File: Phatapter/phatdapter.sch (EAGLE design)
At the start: 16 parts, among them J1 RASPBERRYPI-40-PIN-GPIO_SMD_M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, J2 RASPBERRYPI-40-PIN-GPIO_RIGHT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, J3 QWIIC_RIGHT_ANGLE, J5 QWIIC_RIGHT_ANGLE

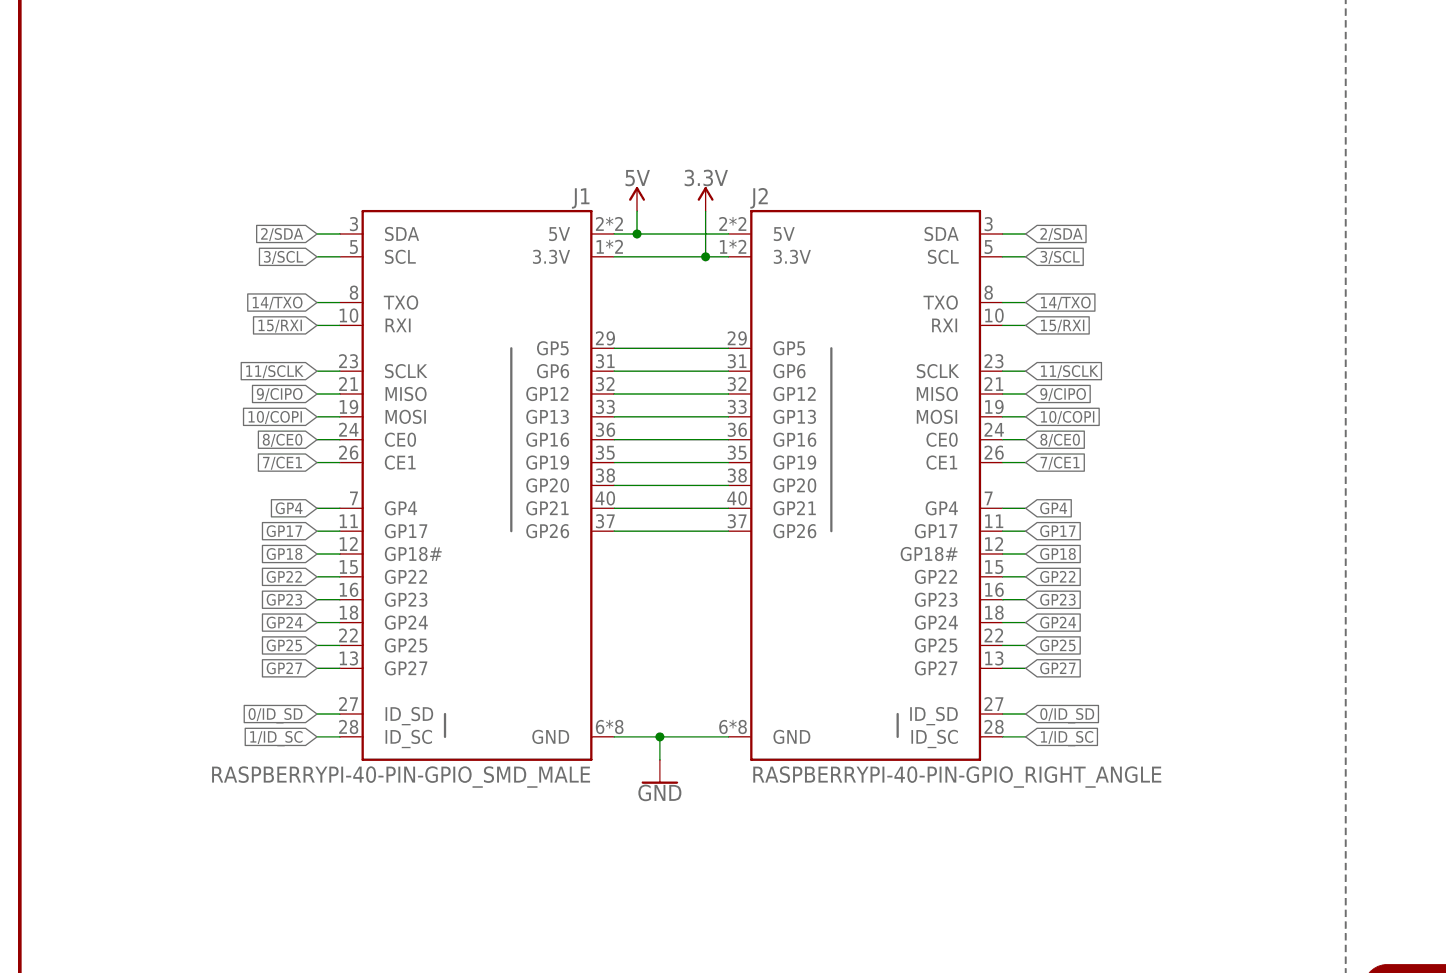
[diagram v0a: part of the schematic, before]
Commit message: Updates symbol which required an entire reroute of the board
* Adds "qwiic mount" silk
* moves Qwiic connector "lower" on the board to align with standoffs
* Adds standoffs for micro-hats
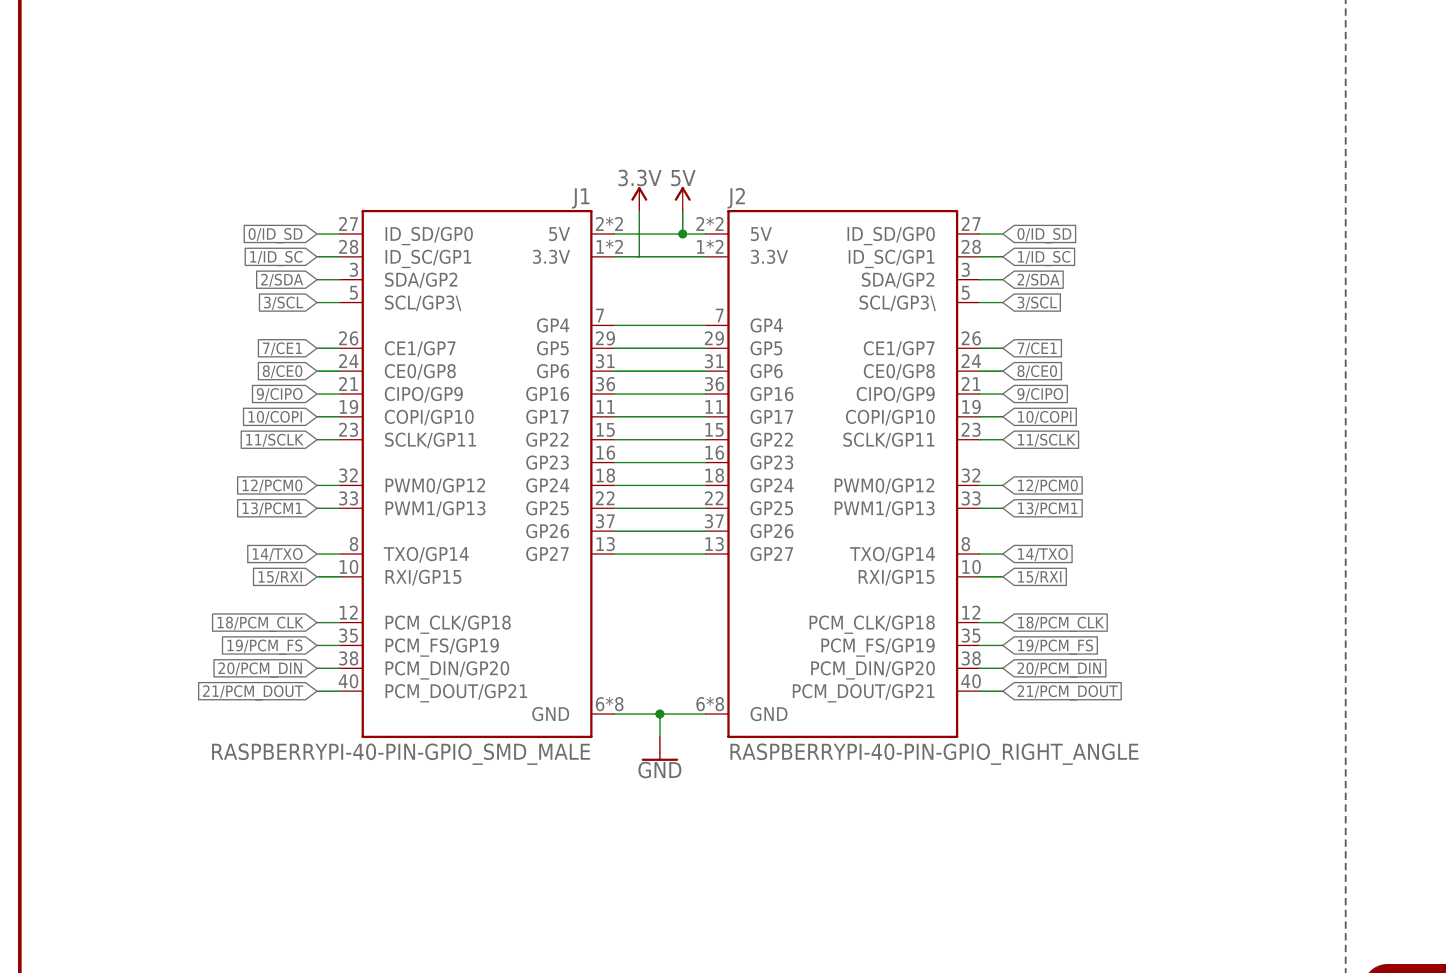
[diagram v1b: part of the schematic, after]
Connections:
- removed net GP12: J1.GP12, J2.GP12
- removed net GP13: J1.GP13, J2.GP13
- removed net GP18: J1.GP18#, J2.GP18#
- removed net GP19: J1.GP19, J2.GP19
- removed net GP20: J1.GP20, J2.GP20
- removed net GP21: J1.GP21, J2.GP21
- new net 12/PCM0: J1.PWM0/GP12, J2.PWM0/GP12
- new net 13/PCM1: J1.PWM1/GP13, J2.PWM1/GP13
- new net 18/PCM_CLK: J1.PCM_CLK/GP18, J2.PCM_CLK/GP18
- new net 19/PCM_FS: J1.PCM_FS/GP19, J2.PCM_FS/GP19
- new net 20/PCM_DIN: J1.PCM_DIN/GP20, J2.PCM_DIN/GP20
- new net 21/PCM_DOUT: J1.PCM_DOUT/GP21, J2.PCM_DOUT/GP21
- net 0/ID_SD: now also J1.ID_SD/GP0, J2.ID_SD/GP0; no longer J1.ID_SD, J2.ID_SD
- net 1/ID_SC: now also J1.ID_SC/GP1, J2.ID_SC/GP1; no longer J1.ID_SC, J2.ID_SC
- net 10/COPI: now also J1.COPI/GP10, J2.COPI/GP10; no longer J1.MOSI, J2.MOSI
- net 11/SCLK: now also J1.SCLK/GP11, J2.SCLK/GP11; no longer J1.SCLK, J2.SCLK
- net 14/TXO: now also J1.TXO/GP14, J2.TXO/GP14; no longer J1.TXO, J2.TXO
- net 15/RXI: now also J1.RXI/GP15, J2.RXI/GP15; no longer J1.RXI, J2.RXI
- net 2/SDA: now also J1.SDA/GP2, J2.SDA/GP2; no longer J1.SDA, J2.SDA
- net 3/SCL: now also J1.SCL/GP3\, J2.SCL/GP3\; no longer J1.SCL, J2.SCL
- net 7/CE1: now also J1.CE1/GP7, J2.CE1/GP7; no longer J1.CE1, J2.CE1
- net 8/CE0: now also J1.CE0/GP8, J2.CE0/GP8; no longer J1.CE0, J2.CE0
- net 9/CIPO: now also J1.CIPO/GP9, J2.CIPO/GP9; no longer J1.MISO, J2.MISO

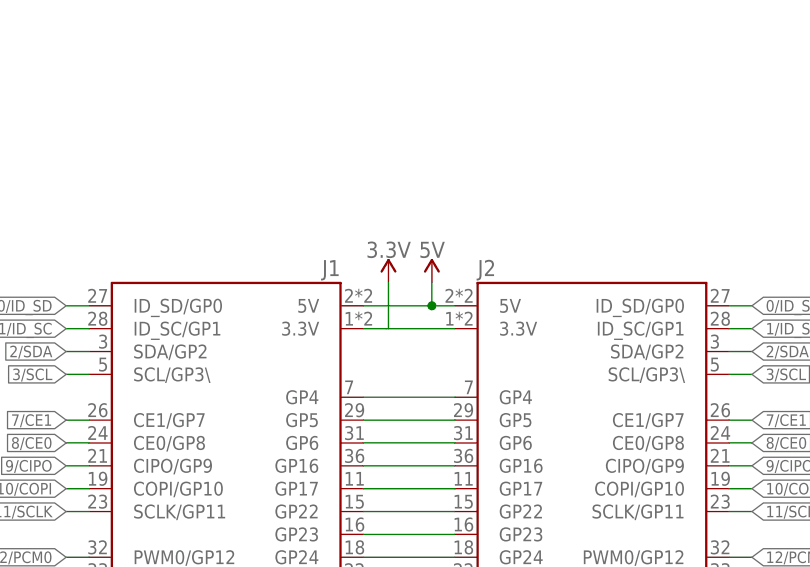
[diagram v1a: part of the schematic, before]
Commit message: Swaps the rows of PTH holes on the right angle connector
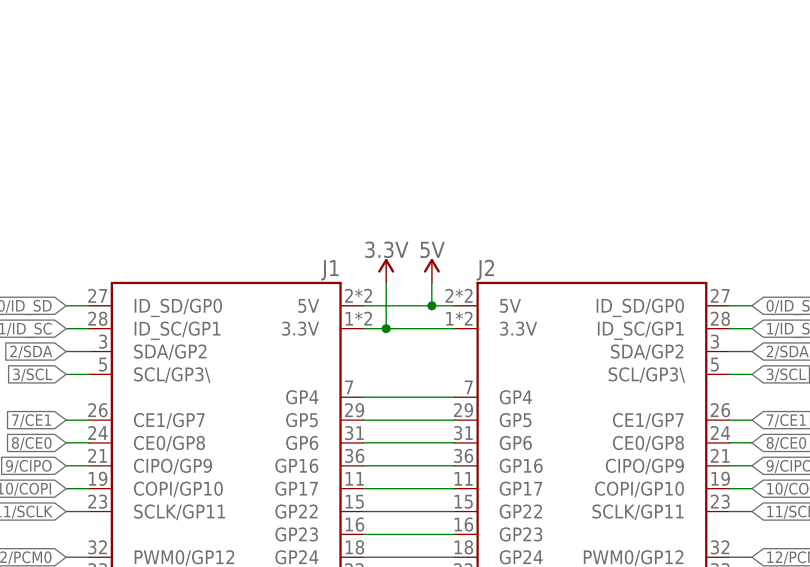
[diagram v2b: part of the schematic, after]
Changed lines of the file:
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@@
 <attribute name="VALUE" x="73.66" y="129.794" size="1.778" layer="96" align="bottom-center"/>
 </instance>
-<instance part="SUPPLY2" gate="G$1" x="68.834" y="127" smashed="yes">
-<attribute name="VALUE" x="68.834" y="129.794" size="1.778" layer="96" align="bottom-center"/>
+<instance part="SUPPLY2" gate="G$1" x="68.58" y="127" smashed="yes">
+<attribute name="VALUE" x="68.58" y="129.794" size="1.778" layer="96" align="bottom-center"/>
 </instance>
 <instance part="J3" gate="G$1" x="193.04" y="124.46" smashed="yes">
@@
 <wire x1="66.04" y1="121.92" x2="68.58" y2="121.92" width="0.1524" layer="91"/>
 <pinref part="SUPPLY2" gate="G$1" pin="3.3V"/>
-<wire x1="68.834" y1="121.92" x2="76.2" y2="121.92" width="0.1524" layer="91"/>
-<wire x1="68.58" y1="121.92" x2="68.834" y2="121.92" width="0.1524" layer="91"/>
-<wire x1="68.834" y1="121.92" x2="68.834" y2="127" width="0.1524" layer="91"/>
+<wire x1="68.58" y1="121.92" x2="76.2" y2="121.92" width="0.1524" layer="91"/>
+<wire x1="68.58" y1="127" x2="68.58" y2="121.92" width="0.1524" layer="91"/>
+<junction x="68.58" y="121.92"/>
 </segment>
 </net>

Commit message: Adds name to board
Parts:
- LOGO2: value SFE_LOGO_NAME_FLAME.4_INCH -> SFE_LOGO_NAME_FLAME.2_INCH; device SparkFun-Aesthetics:SFE_LOGO_NAME_FLAME.4_INCH -> SparkFun-Aesthetics:SFE_LOGO_NAME_FLAME.2_INCH
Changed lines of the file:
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@@
 <part name="SUPPLY3" library="SparkFun-PowerSymbols" deviceset="3.3V" device=""/>
 <part name="LOGO1" library="SparkFun-Aesthetics" deviceset="QWIIC_LOGO" device="_5MM"/>
-<part name="LOGO2" library="SparkFun-Aesthetics" deviceset="SFE_LOGO_NAME_FLAME" device=".4_INCH"/>
+<part name="LOGO2" library="SparkFun-Aesthetics" deviceset="SFE_LOGO_NAME_FLAME" device=".2_INCH" value="SFE_LOGO_NAME_FLAME.2_INCH"/>
 <part name="LOGO3" library="SparkFun-Aesthetics" deviceset="OSHW-LOGO" device="M"/>
 </parts>
